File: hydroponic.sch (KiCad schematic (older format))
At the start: 98 parts, among them J1 12V DC, J10 Matrix key, J11 ds18b20, J12 ec, J13 bh1750, J14 dht11, J2 vi, J3 po, J4 pa, J5 pb, J6 vo, J7 fa, J8 lt, J9 lcd, U1 ULN2003, U10 LM324, U11 AMP4953, U12 AMP4953, U13 AMP4953, U14 LM324, U2 STM32duino, U3 LM2596T-5V, U4 AMP4953, U5 nodemcu, U6 LM1117-3.3, U7 AMP4953, U8 AMP4953, U9 AMP4953

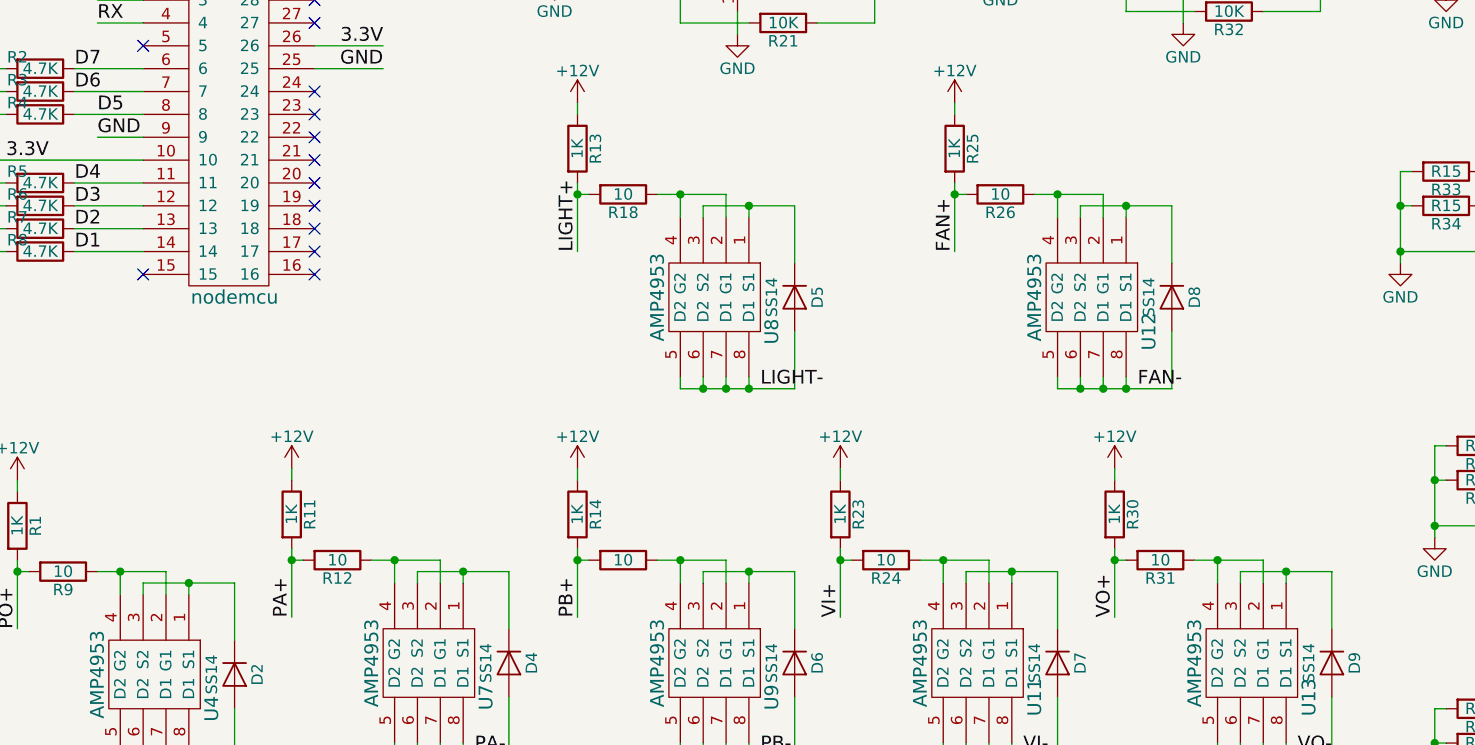
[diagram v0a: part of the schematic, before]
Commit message: add net 12v to AMP4953
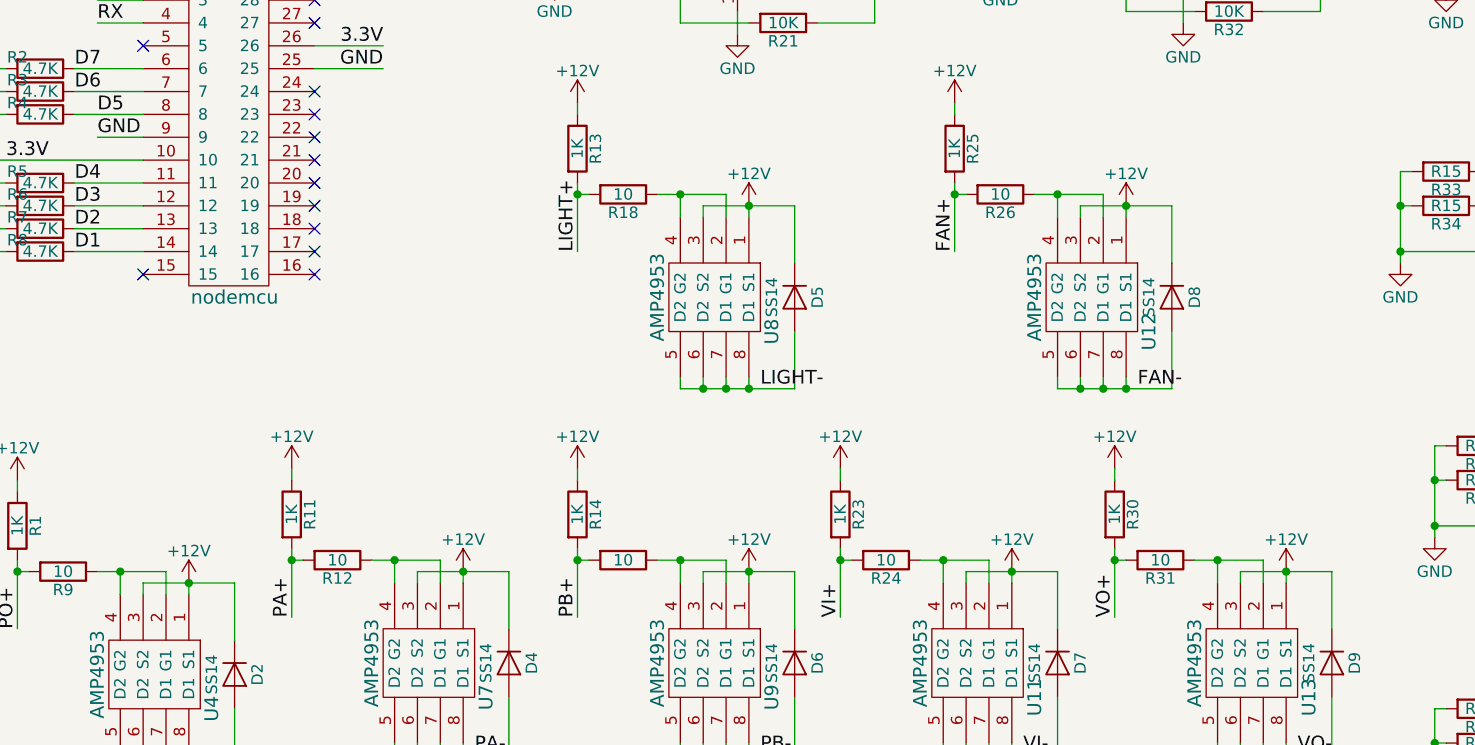
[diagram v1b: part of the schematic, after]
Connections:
- net +12V: now also D2.1 (K), D4.1 (K), D5.1 (K), D6.1 (K), D7.1 (K), D8.1 (K), D9.1 (K), U11.1 (S1), U11.3 (S2), U12.1 (S1), U12.3 (S2), U13.1 (S1), U13.3 (S2), U4.1 (S1), U4.3 (S2), U7.1 (S1), U7.3 (S2), U8.1 (S1), U8.3 (S2), U9.1 (S1), U9.3 (S2)
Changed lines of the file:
@@
 LIBS:contrib
 LIBS:valves
+LIBS:ac-dc
+LIBS:Altera
+LIBS:analog_devices
+LIBS:Battery_Management
+LIBS:bbd
+LIBS:Bosch
+LIBS:brooktre
+LIBS:Connector
+LIBS:dc-dc
+LIBS:Decawave
+LIBS:Diode
+LIBS:Display
+LIBS:driver_gate
+LIBS:DSP_Microchip_DSPIC33
+LIBS:elec-unifil
+LIBS:ESD_Protection
+LIBS:Espressif
+LIBS:FPGA_Actel
+LIBS:ftdi
+LIBS:gennum
+LIBS:Graphic
+LIBS:hc11
+LIBS:infineon
+LIBS:intersil
+LIBS:ir
+LIBS:Lattice
+LIBS:LED
+LIBS:LEM
+LIBS:Logic_74xgxx
+LIBS:Logic_74xx
+LIBS:Logic_CMOS_4000
+LIBS:Logic_CMOS_IEEE
+LIBS:logic_programmable
+LIBS:Logic_TTL_IEEE
+LIBS:maxim
+LIBS:MCU_Microchip_PIC10
+LIBS:MCU_Microchip_PIC12
+LIBS:MCU_Microchip_PIC16
+LIBS:MCU_Microchip_PIC18
+LIBS:MCU_Microchip_PIC24
+LIBS:MCU_Microchip_PIC32
+LIBS:MCU_NXP_Kinetis
+LIBS:MCU_NXP_LPC
+LIBS:MCU_NXP_S08
+LIBS:MCU_Parallax
+LIBS:MCU_ST_STM8
+LIBS:MCU_ST_STM32
+LIBS:MCU_Texas_MSP430
+LIBS:Mechanical
+LIBS:modules
+LIBS:Motor
+LIBS:motor_drivers
+LIBS:nordicsemi
+LIBS:nxp
+LIBS:onsemi
+LIBS:Oscillators
+LIBS:Power_Management
+LIBS:powerint
+LIBS:pspice
+LIBS:references
+LIBS:Relay
+LIBS:RF_Bluetooth
+LIBS:rfcom
+LIBS:RFSolutions
+LIBS:Sensor_Current
+LIBS:Sensor_Humidity
+LIBS:sensors
+LIBS:silabs
+LIBS:supertex
+LIBS:Switch
+LIBS:Transformer
+LIBS:Transistor
+LIBS:triac_thyristor
+LIBS:Valve
+LIBS:video
+LIBS:wiznet
+LIBS:Worldsemi
+LIBS:Xicor
+LIBS:zetex
+LIBS:Zilog
+LIBS:Symbols_DCDC-ACDC-Converter_RevC_20Jul2012
+LIBS:Symbols_EN60617_13Mar2013
+LIBS:Symbols_EN60617-10_HF-Radio_DRAFT_12Sep2013
+LIBS:Symbols_ICs-Diskrete_RevD10
+LIBS:Symbols_ICs-Opto_RevB_16Sep2013
+LIBS:Symbols_Microcontroller_Philips-NXP_RevA_06Oct2013
+LIBS:Symbols_Socket-DIN41612_RevA
+LIBS:Symbols_Transformer-Diskrete_RevA
+LIBS:SymbolsSimilarEN60617+oldDIN617-RevE8
+LIBS:all
 LIBS:hydroponic-cache
 EELAYER 25 0
@@
 Text Label 700  3450 0    60   ~ 0
 LCD_D7
+$Comp
+L +12V #PWR?
+U 1 1 5A446D48
+P 3700 5150
+F 0 "#PWR?" H 3700 5000 50  0001 C CNN
+F 1 "+12V" H 3700 5290 50  0000 C CNN
+F 2 "" H 3700 5150 50  0001 C CNN
+F 3 "" H 3700 5150 50  0001 C CNN
+	1    3700 5150
+	1    0    0    -1
+$EndComp
+$Comp
+L +12V #PWR?
+U 1 1 5A446EEF
+P 4900 5100
+F 0 "#PWR?" H 4900 4950 50  0001 C CNN
+F 1 "+12V" H 4900 5240 50  0000 C CNN
+F 2 "" H 4900 5100 50  0001 C CNN
+F 3 "" H 4900 5100 50  0001 C CNN
+	1    4900 5100
+	1    0    0    -1
+$EndComp
+$Comp
+L +12V #PWR?
+U 1 1 5A4471CB
+P 6150 5100
+F 0 "#PWR?" H 6150 4950 50  0001 C CNN
+F 1 "+12V" H 6150 5240 50  0000 C CNN
+F 2 "" H 6150 5100 50  0001 C CNN
+F 3 "" H 6150 5100 50  0001 C CNN
+	1    6150 5100
+	1    0    0    -1
+$EndComp
+$Comp
+L +12V #PWR?
+U 1 1 5A447440
+P 7300 5100
+F 0 "#PWR?" H 7300 4950 50  0001 C CNN
+F 1 "+12V" H 7300 5240 50  0000 C CNN
+F 2 "" H 7300 5100 50  0001 C CNN
+F 3 "" H 7300 5100 50  0001 C CNN
+	1    7300 5100
+	1    0    0    -1
+$EndComp
+$Comp
+L +12V #PWR?
+U 1 1 5A447580
+P 8500 5100
+F 0 "#PWR?" H 8500 4950 50  0001 C CNN
+F 1 "+12V" H 8500 5240 50  0000 C CNN
+F 2 "" H 8500 5100 50  0001 C CNN
+F 3 "" H 8500 5100 50  0001 C CNN
+	1    8500 5100
+	1    0    0    -1
+$EndComp
+$Comp
+L +12V #PWR?
+U 1 1 5A4478C3
+P 7800 3500
+F 0 "#PWR?" H 7800 3350 50  0001 C CNN
+F 1 "+12V" H 7800 3640 50  0000 C CNN
+F 2 "" H 7800 3500 50  0001 C CNN
+F 3 "" H 7800 3500 50  0001 C CNN
+	1    7800 3500
+	1    0    0    -1
+$EndComp
+$Comp
+L +12V #PWR?
+U 1 1 5A447B38
+P 6150 3500
+F 0 "#PWR?" H 6150 3350 50  0001 C CNN
+F 1 "+12V" H 6150 3640 50  0000 C CNN
+F 2 "" H 6150 3500 50  0001 C CNN
+F 3 "" H 6150 3500 50  0001 C CNN
+	1    6150 3500
+	1    0    0    -1
+$EndComp
 $EndSCHEMATC
